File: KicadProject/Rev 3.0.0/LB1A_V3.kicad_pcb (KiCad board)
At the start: 6 copper layers, 45 x 45 mm, 188 parts, among them J601 2337019-1, J602 2337019-1, U101 STM32MP157CAA3, U201 AS4C256M16D3LC-12BCN, U401 STPMIC1xPQR, U501 S40FC004C1B2C00000, U601 LBEE59B1LV-278, U701 DF40C-70DP-0.4V(51), U702 DF40C-100DP-0.4V(51), U703 DF40C-100DP-0.4V(51), X101 32.768kHz, Y101 24MHz

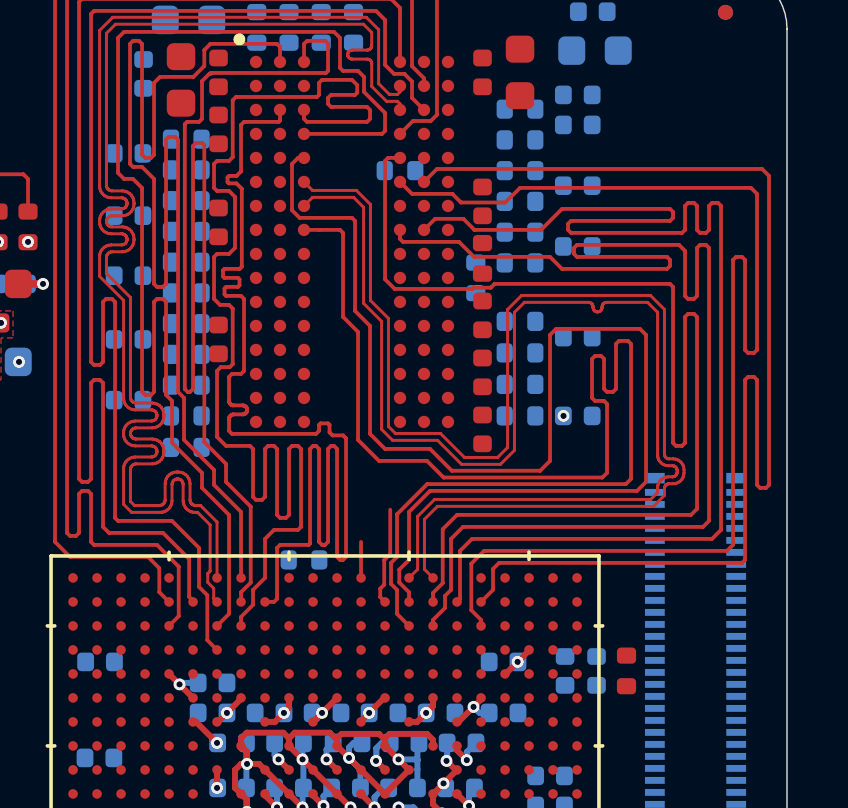
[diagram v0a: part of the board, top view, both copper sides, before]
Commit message: top layer of ddr3l complete
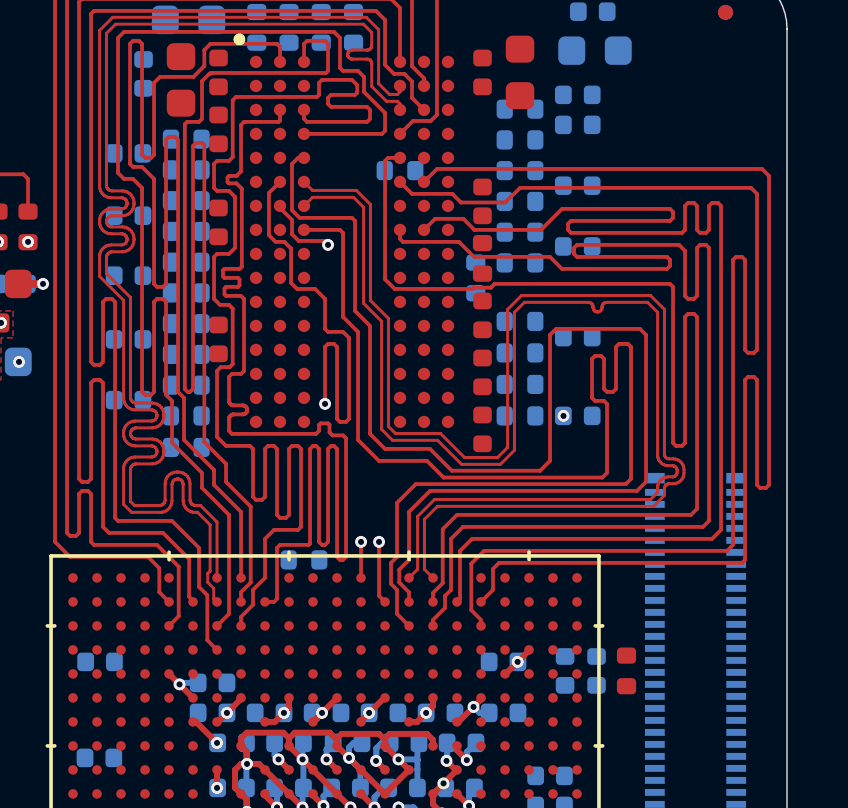
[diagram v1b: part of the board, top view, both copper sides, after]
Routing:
- net /MPU_DDR3L_Memory/DDR_DQ8: track 1.27 -> 42.4 mm, vias 0 -> 2
- net /MPU_DDR3L_Memory/DDR_DQ10: track 3.28 -> 42.3 mm, vias 0 -> 2

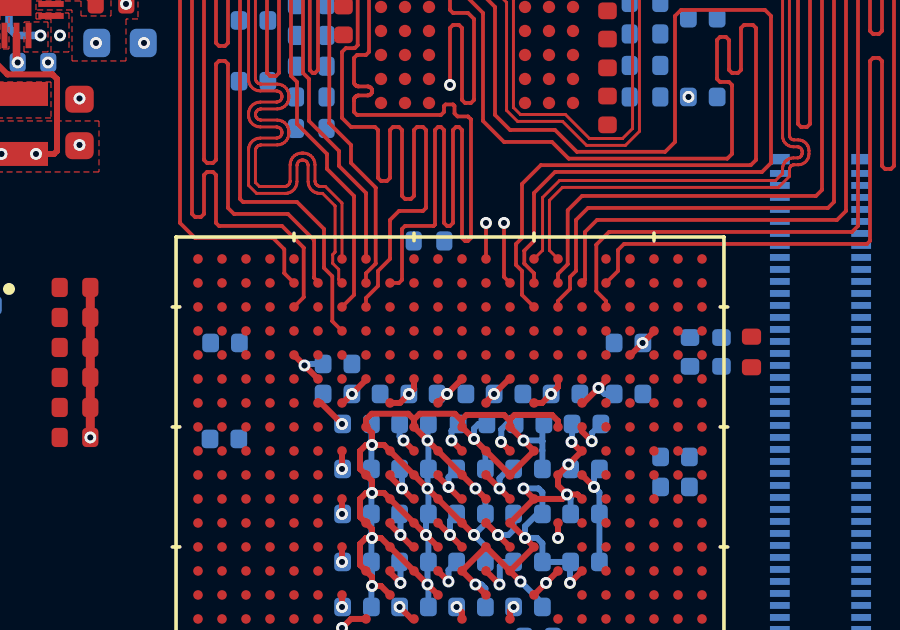
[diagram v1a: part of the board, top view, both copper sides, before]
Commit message: working on ddr3l
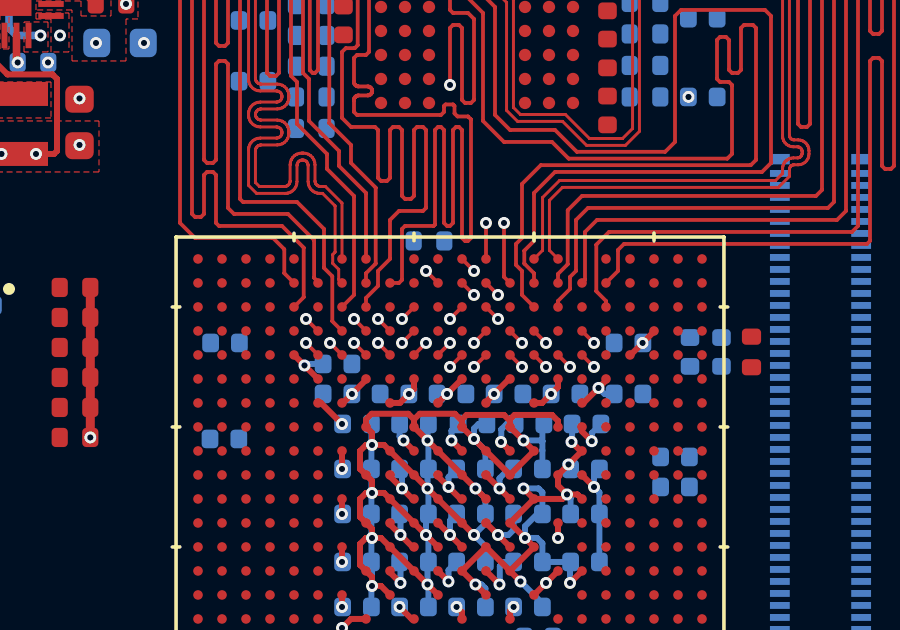
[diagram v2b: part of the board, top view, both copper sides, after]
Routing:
- net /MPU_DDR3L_Memory/DDR_RESETN: track 0.00 -> 0.57 mm, vias 0 -> 1
- net /MPU_DDR3L_Memory/DDR_A7: track 0.00 -> 0.57 mm, vias 0 -> 1
- net /MPU_DDR3L_Memory/DDR_CSN: track 0.00 -> 0.57 mm, vias 0 -> 1
- net /MPU_DDR3L_Memory/DDR_BA2: track 0.00 -> 0.57 mm, vias 0 -> 1
- net /MPU_DDR3L_Memory/DDR_A13: track 0.00 -> 0.57 mm, vias 0 -> 1
- net /MPU_DDR3L_Memory/DDR_A9: track 0.00 -> 0.57 mm, vias 0 -> 1
- net /MPU_DDR3L_Memory/DDR_A5: track 0.00 -> 0.57 mm, vias 0 -> 1
- net /MPU_DDR3L_Memory/DDR_A3: track 0.00 -> 0.57 mm, vias 0 -> 1
- net /MPU_DDR3L_Memory/DDR_A2: track 0.00 -> 0.57 mm, vias 0 -> 1
- net /MPU_DDR3L_Memory/DDR_ODT: track 0.00 -> 0.57 mm, vias 0 -> 1
- net /MPU_DDR3L_Memory/DDR_CASN: track 0.00 -> 0.57 mm, vias 0 -> 1
- net /MPU_DDR3L_Memory/DDR_BA1: track 0.00 -> 0.57 mm, vias 0 -> 1
- net /MPU_DDR3L_Memory/DDR_A8: track 0.00 -> 0.57 mm, vias 0 -> 1
- net /MPU_DDR3L_Memory/DDR_A4: track 0.00 -> 0.57 mm, vias 0 -> 1
- net /MPU_DDR3L_Memory/DDR_A14: track 0.00 -> 0.57 mm, vias 0 -> 1
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
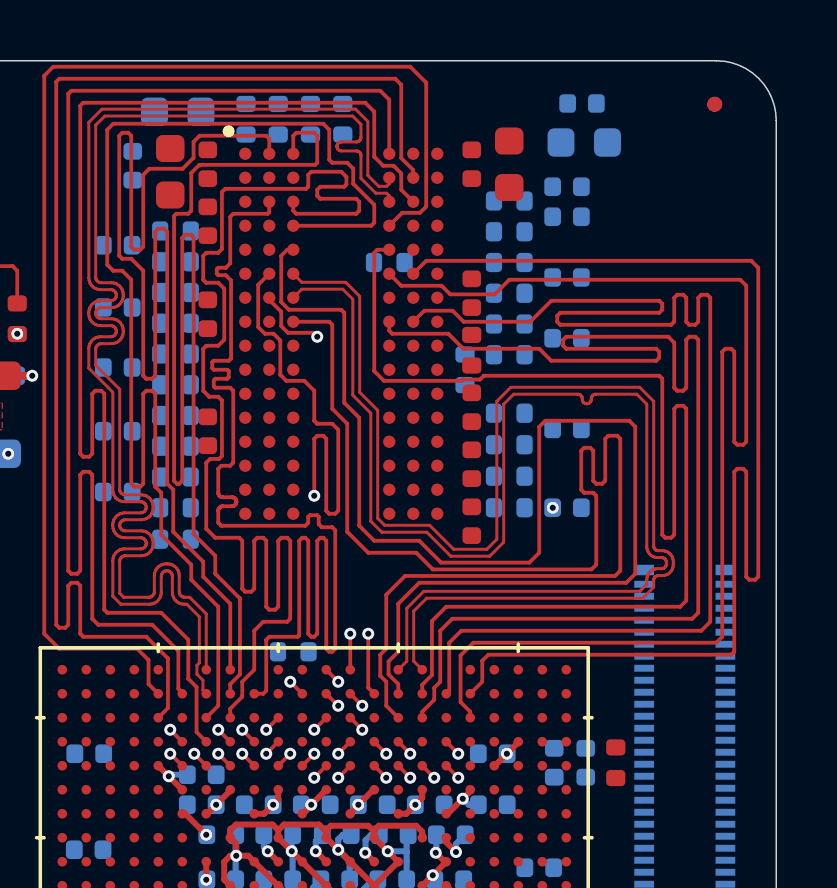
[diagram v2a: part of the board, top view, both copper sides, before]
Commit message: working on ddr3l
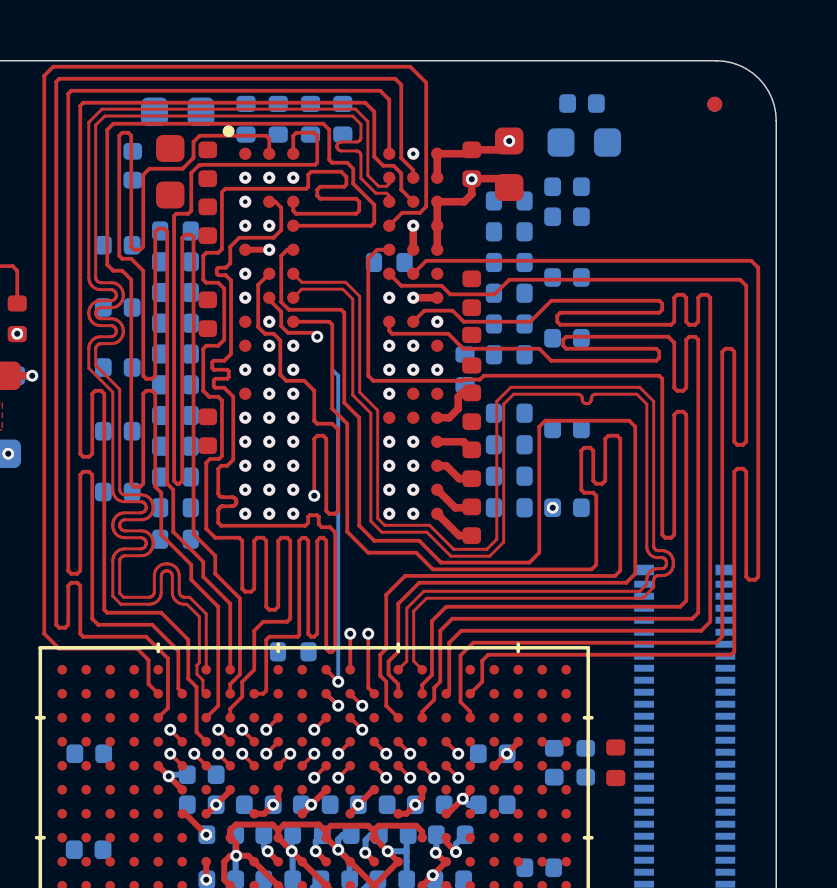
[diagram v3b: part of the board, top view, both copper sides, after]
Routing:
- net /MPU_DDR3L_Memory/DDR_CASN: track 0.57 -> 11.1 mm, vias 1 -> 2
- net GND: track 57.1 -> 67.4 mm, vias 67 -> 80
- net PMIC_VOUT2_VDD_DDR: track 17.6 -> 25.0 mm, vias 10 -> 23
- net /MPU_DDR3L_Memory/DDR_ODT: track 0.57 -> 0.00 mm
- net /MPU_DDR3L_Memory/DDR_WEN: track 0.57 -> 1.08 mm, vias 1 -> 2
- net /MPU_DDR3L_Memory/DDR_RESETN: vias 1 -> 2
- net /MPU_DDR3L_Memory/DDR_RASN: vias 1 -> 2
- net /MPU_DDR3L_Memory/DDR_CSN: vias 1 -> 2
- net /MPU_DDR3L_Memory/DDR_CLK_P: vias 1 -> 2
- net /MPU_DDR3L_Memory/DDR_CLK_N: vias 1 -> 2
- net /MPU_DDR3L_Memory/DDR_CKE: vias 1 -> 2
- net /MPU_DDR3L_Memory/DDR_BA2: vias 1 -> 2
- net /MPU_DDR3L_Memory/DDR_BA1: vias 1 -> 2
- net /MPU_DDR3L_Memory/DDR_BA0: vias 1 -> 2
- net /MPU_DDR3L_Memory/DDR_A9: vias 1 -> 2
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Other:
- rule via_min_drill: 0.2 -> 0.15

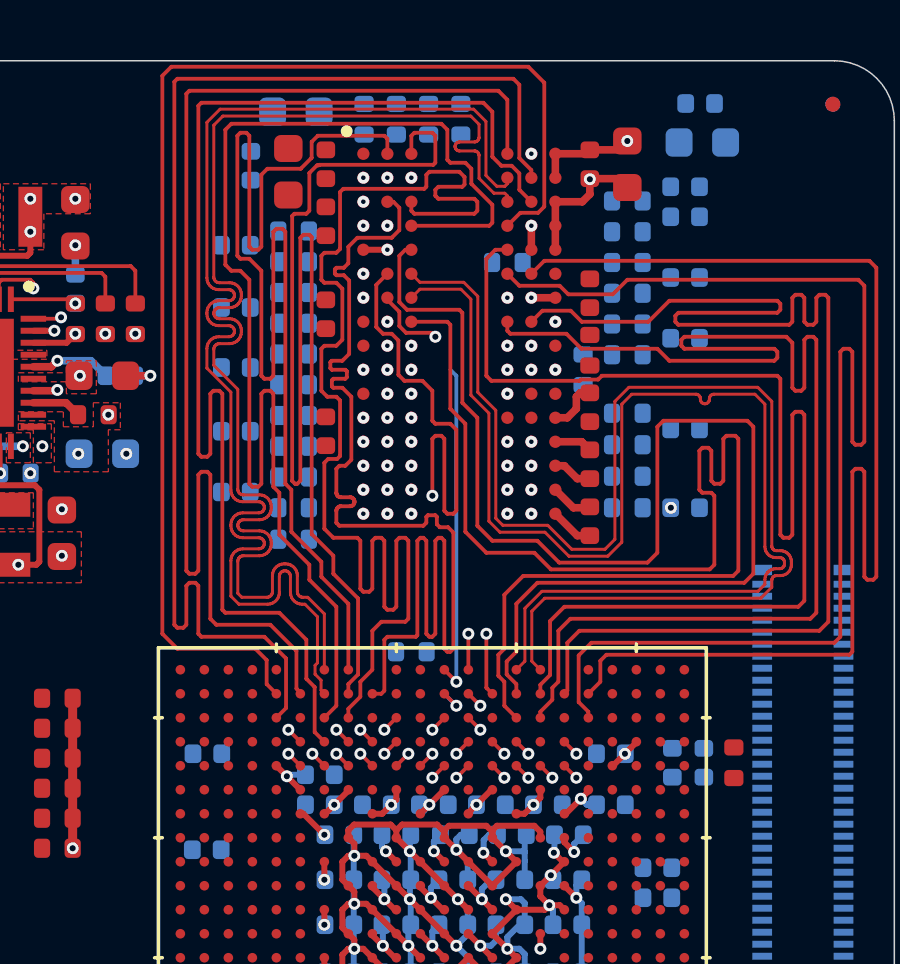
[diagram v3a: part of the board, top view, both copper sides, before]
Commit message: some updates on ram routing
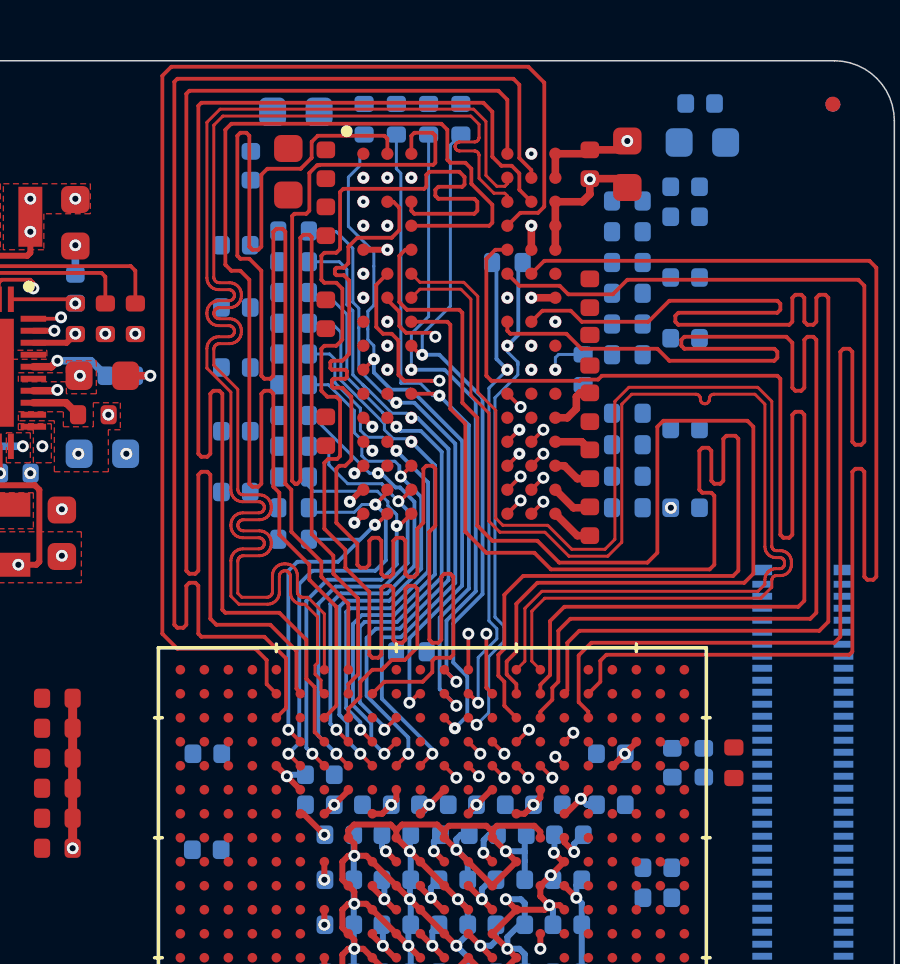
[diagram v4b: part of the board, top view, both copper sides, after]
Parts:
- moved R203 1.03 mm to (136.1, 89.7)
- moved R215 1.03 mm to (136.1, 90.7)
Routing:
- net /MPU_DDR3L_Memory/DDR_RASN: track 0.57 -> 23.2 mm
- net /MPU_DDR3L_Memory/DDR_ODT: track 0.00 -> 22.5 mm, vias 1 -> 2
- net /MPU_DDR3L_Memory/DDR_CSN: track 0.57 -> 22.8 mm
- net /MPU_DDR3L_Memory/DDR_BA2: track 0.57 -> 22.2 mm
- net /MPU_DDR3L_Memory/DDR_WEN: track 1.08 -> 22.7 mm
- net /MPU_DDR3L_Memory/DDR_BA0: track 0.57 -> 20.3 mm
- net /MPU_DDR3L_Memory/DDR_A0: track 0.57 -> 19.6 mm
- net /MPU_DDR3L_Memory/DDR_A2: track 0.57 -> 18.2 mm
- net /MPU_DDR3L_Memory/DDR_A3: track 0.57 -> 18.0 mm
- net /MPU_DDR3L_Memory/DDR_CLK_P: track 0.57 -> 17.2 mm
- net /MPU_DDR3L_Memory/DDR_A9: track 0.57 -> 16.3 mm
- net /MPU_DDR3L_Memory/DDR_CLK_N: track 0.57 -> 16.0 mm
- net /MPU_DDR3L_Memory/DDR_A5: track 0.57 -> 15.4 mm
- net /MPU_DDR3L_Memory/DDR_A13: track 0.57 -> 15.3 mm
- net /MPU_DDR3L_Memory/DDR_A7: track 0.57 -> 14.9 mm
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
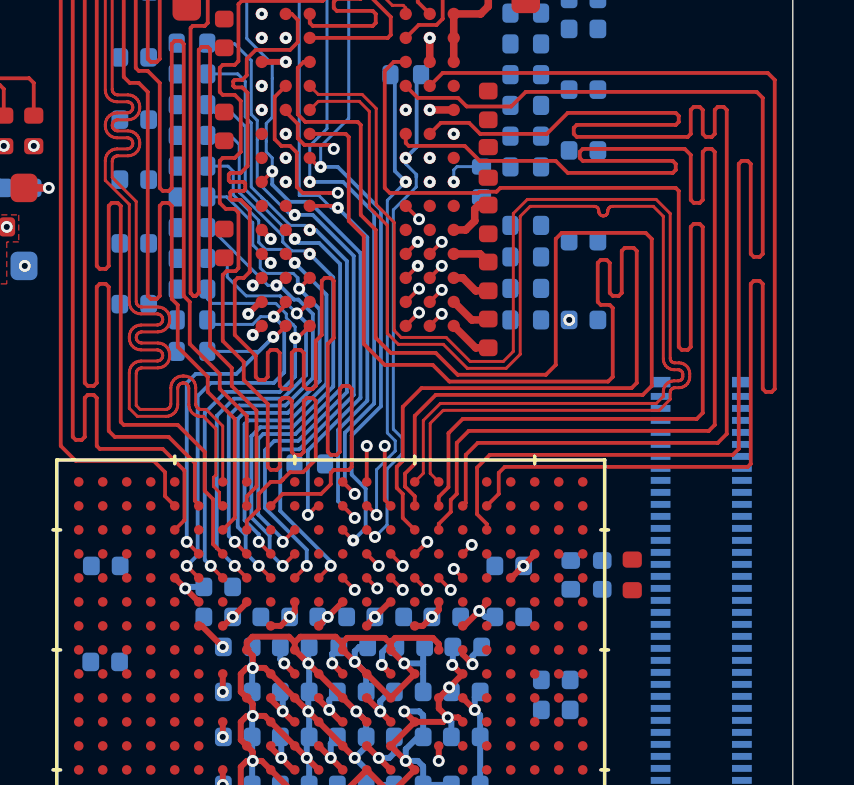
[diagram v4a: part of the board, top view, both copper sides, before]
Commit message: ddr3l cleaning required
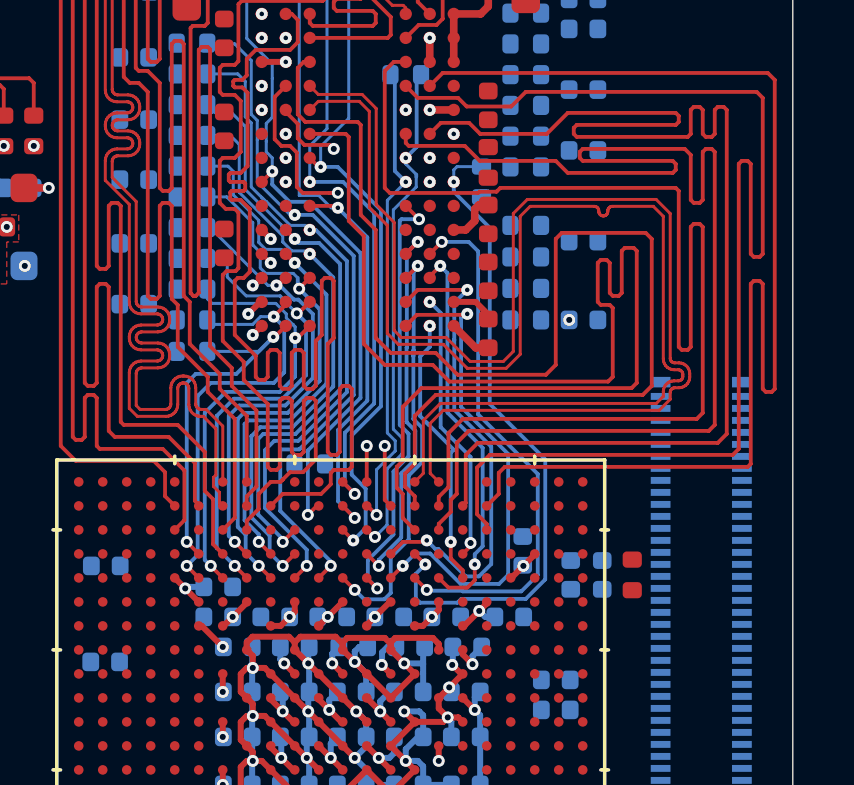
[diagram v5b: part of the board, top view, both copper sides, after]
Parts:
- moved C331 0.67 mm to (136.0, 107.6), turned to 90 degrees
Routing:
- net /MPU_DDR3L_Memory/DDR_CKE: track 1.95 -> 22.4 mm
- net /MPU_DDR3L_Memory/DDR_BA1: track 1.13 -> 18.0 mm
- net /MPU_DDR3L_Memory/DDR_A14: track 1.20 -> 16.6 mm
- net /MPU_DDR3L_Memory/DDR_A11: track 1.27 -> 16.3 mm
- net /MPU_DDR3L_Memory/DDR_A10: track 1.12 -> 14.9 mm
- net /MPU_DDR3L_Memory/DDR_A1: track 1.13 -> 14.2 mm
- net /MPU_DDR3L_Memory/DDR_A4: track 1.13 -> 13.2 mm
- net /MPU_DDR3L_Memory/DDR_A12: track 1.13 -> 12.7 mm
- net /MPU_DDR3L_Memory/DDR_A8: track 0.85 -> 9.33 mm
- net /MPU_DDR3L_Memory/DDR_A6: track 1.25 -> 9.27 mm
- net GND: track 68.6 -> 67.3 mm
- net PMIC_VOUT2_VDD_DDR: track 26.1 -> 24.9 mm

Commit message: some cleaning done
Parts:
- C207, C330, R210: moved to F.Cu
- moved C331 3.21 mm to (139.2, 107.9), turned to 0 degrees
- moved R210 2.84 mm to (131.1, 102.9), turned to 90 degrees
- moved C330 2.79 mm to (139.6, 110.3), turned to 270 degrees
- moved C207 2.15 mm to (139.7, 106.5)
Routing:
- net /MPU_DDR3L_Memory/DDR_RESETN: track 12.4 -> 25.8 mm
- net /MPU_DDR3L_Memory/DDR_A7: track 14.9 -> 27.7 mm
- net /MPU_DDR3L_Memory/DDR_A13: track 15.3 -> 28.0 mm
- net /MPU_DDR3L_Memory/DDR_A9: track 16.3 -> 28.9 mm
- net /MPU_DDR3L_Memory/DDR_A5: track 15.4 -> 28.0 mm
- net /MPU_DDR3L_Memory/DDR_A2: track 18.2 -> 30.4 mm
- net /MPU_DDR3L_Memory/DDR_A3: track 18.0 -> 29.9 mm
- net /MPU_DDR3L_Memory/DDR_A0: track 19.6 -> 31.3 mm
- net /MPU_DDR3L_Memory/DDR_BA0: track 20.3 -> 31.6 mm
- net /MPU_DDR3L_Memory/DDR_CSN: track 22.8 -> 12.1 mm
- net /MPU_DDR3L_Memory/DDR_BA2: track 22.2 -> 32.1 mm
- net /MPU_DDR3L_Memory/DDR_ODT: track 22.5 -> 23.6 mm

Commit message: little more done
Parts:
- moved R222 0.10 mm to (134.6, 95.2)
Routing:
- net /MPU_DDR3L_Memory/DDR_A4: track 13.2 -> 26.1 mm
- net /MPU_DDR3L_Memory/DDR_BA1: track 18.0 -> 30.7 mm
- net /MPU_DDR3L_Memory/DDR_A14: track 16.6 -> 25.8 mm
- net /MPU_DDR3L_Memory/DDR_A11: track 16.3 -> 24.5 mm
- net /MPU_DDR3L_Memory/DDR_CKE: track 22.4 -> 27.6 mm

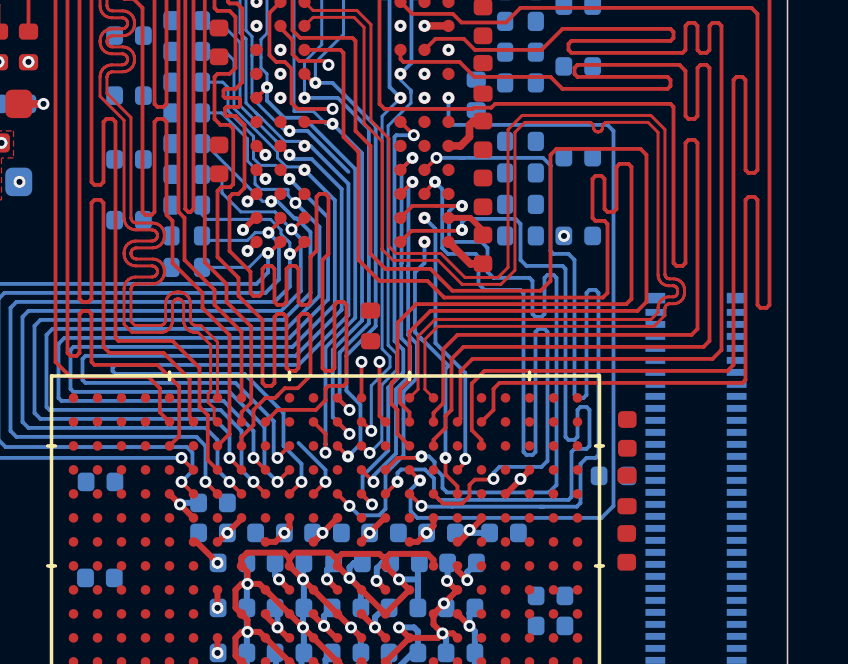
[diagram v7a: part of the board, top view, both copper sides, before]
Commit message: some more traces done
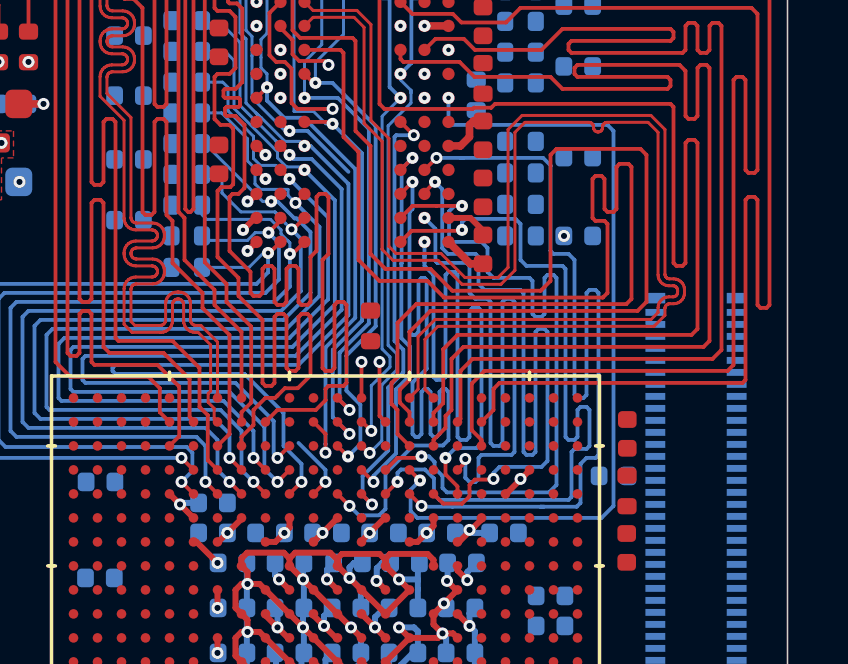
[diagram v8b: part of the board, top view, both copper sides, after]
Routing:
- net /MPU_DDR3L_Memory/DDR_A8: track 9.33 -> 27.0 mm
- net /MPU_DDR3L_Memory/DDR_A6: track 9.27 -> 23.7 mm
- net /MPU_DDR3L_Memory/DDR_A1: track 14.2 -> 26.5 mm
